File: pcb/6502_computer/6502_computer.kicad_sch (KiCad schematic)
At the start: 44 parts, among them J1 Conn_02x04_Odd_Even, J2 USB_B, J3 Conn_02x20_Odd_Even, J4 Conn_01x04, J5 Conn_01x02, SW1 SW_Push, SW2 SW_Push, SW3 SW_Push, U1 6502, U10 CH340N, U11 MC6840, U2 6551, U3 74LS139, U4 74LS138, U5 CY62256-70PC, U6 27C64, U7 74LS00, U8 DS1813-5+, U9 74LS93, X1 ACO-xxxMHz, Y1 1.8432MHz

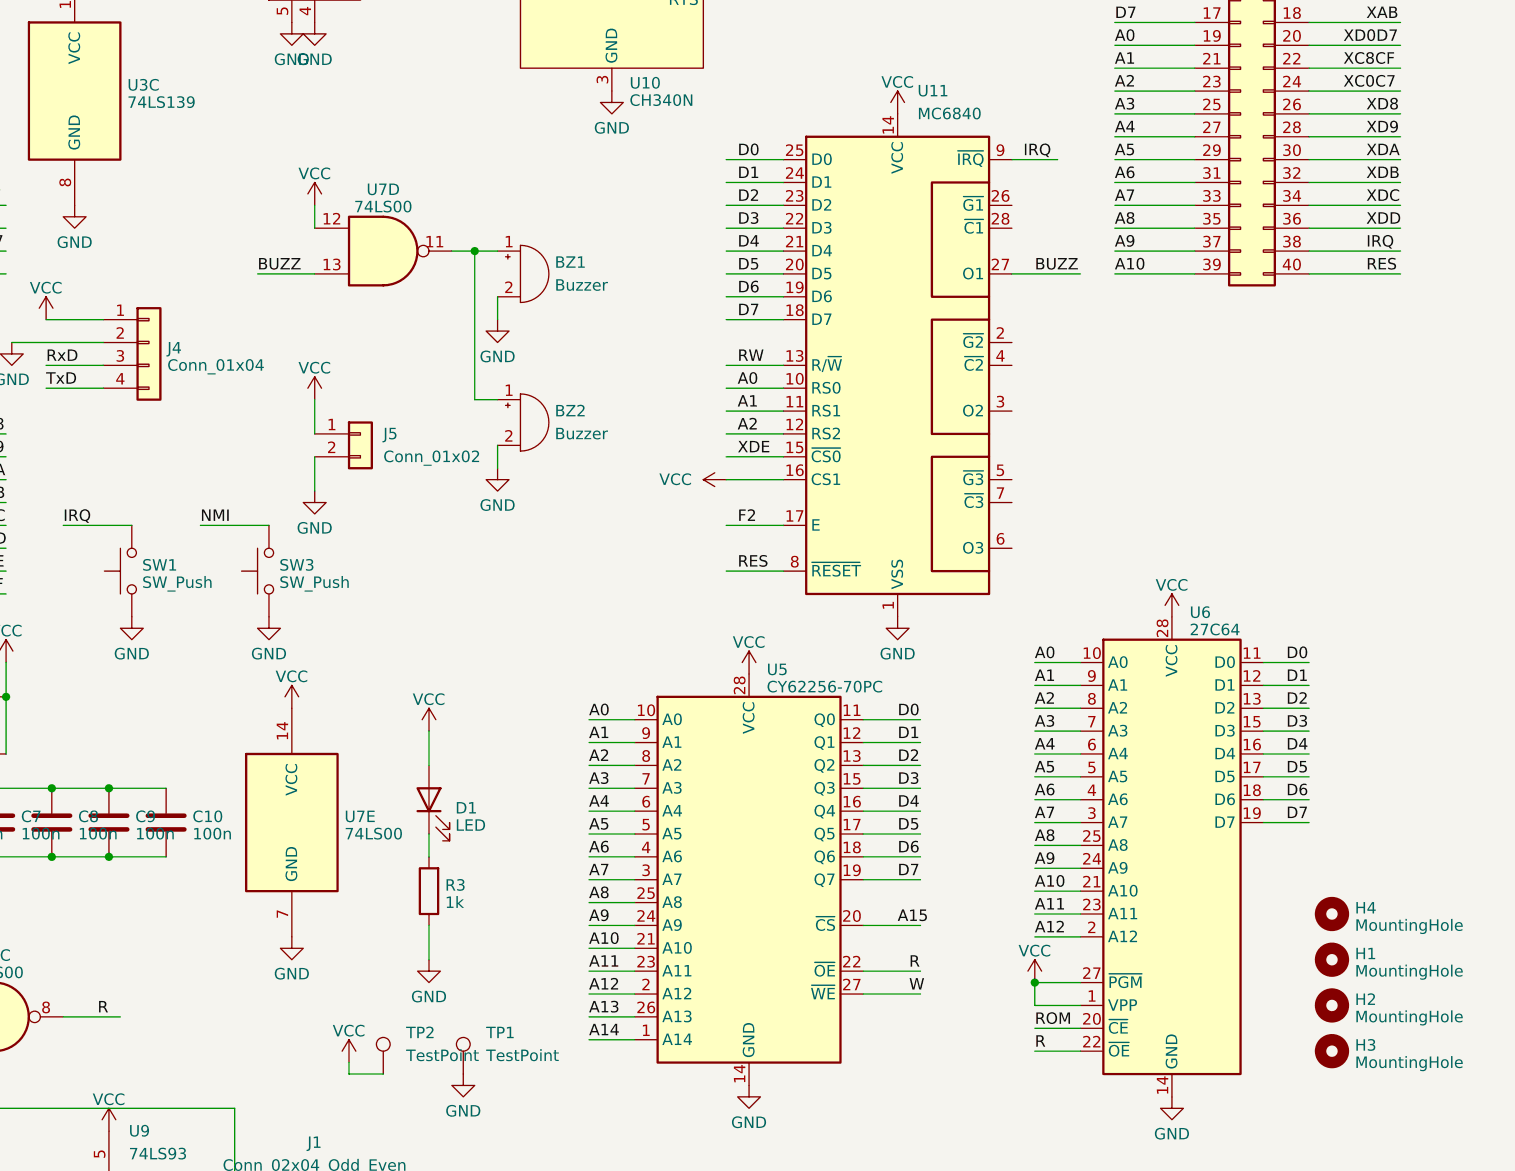
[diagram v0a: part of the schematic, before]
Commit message: added timer outputs from 6840
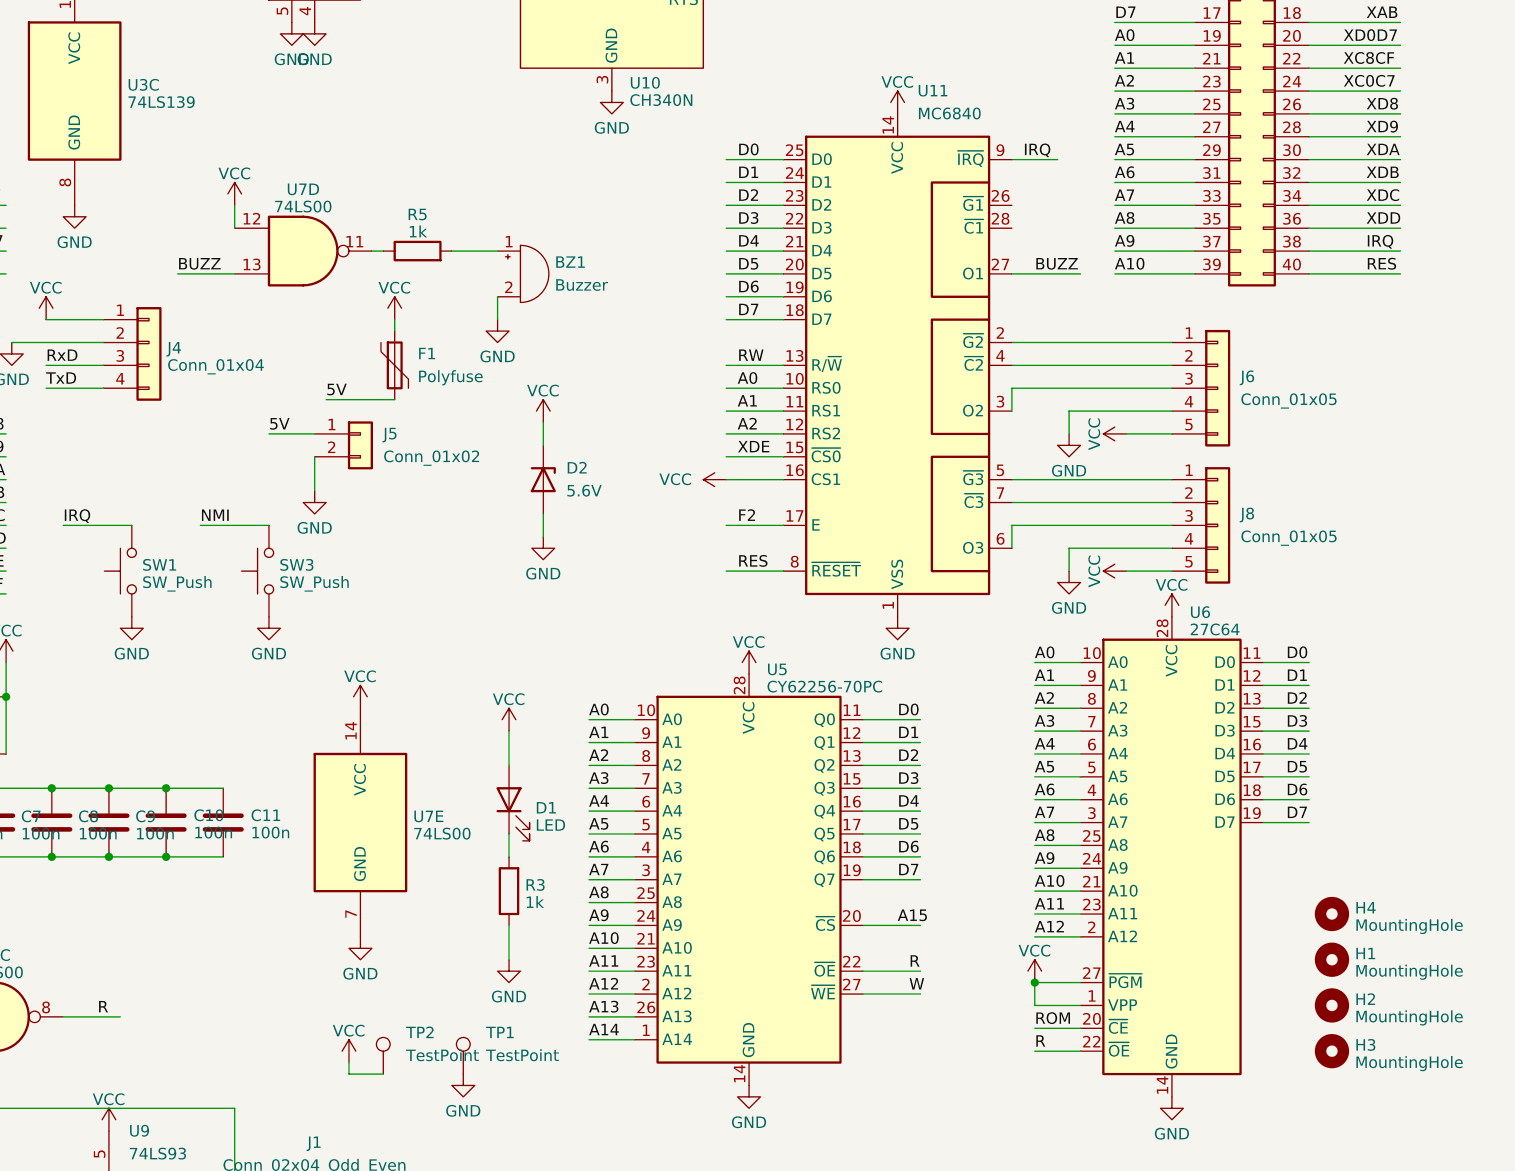
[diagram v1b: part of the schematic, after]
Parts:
- removed BZ2: Buzzer, Buzzer_Beeper:Buzzer_12x9.5RM7.6, symbol Device:Buzzer
- added C11: 100n, Capacitor_SMD:C_0805_2012Metric, symbol Device:C
- added D2: 5.6V, Diode_SMD:D_SOD-123, symbol Device:D_Zener
- added F1: Polyfuse, Fuse:Fuse_0805_2012Metric, symbol Device:Polyfuse
- added J6, J8: Conn_01x05, Connector_Molex:Molex_KK-254_AE-6410-05A_1x05_P2.54mm_Vertical, symbol Connector_Generic:Conn_01x05
- added R5: 1k, Resistor_SMD:R_0805_2012Metric, symbol Device:R
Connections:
- net GND: now also C11.1, D2.2 (A), J6.4 (Pin_4), J8.4 (Pin_4)
- net VCC: now also C11.2, D2.1 (K), F1.1, J6.5 (Pin_5), J8.5 (Pin_5); no longer J5.1 (Pin_1)
- net at U7.11: now also R5.1; no longer BZ1.1 (+)
- net at U11.2 (~{G2}): now also J6.1 (Pin_1)
- net at U11.3 (O2): now also J6.3 (Pin_3)
- net at U11.4 (~{C2}): now also J6.2 (Pin_2)
- net at U11.5 (~{G3}): now also J8.1 (Pin_1)
- net at U11.6 (O3): now also J8.3 (Pin_3)
- net at U11.7 (~{C3}): now also J8.2 (Pin_2)
- new net: BZ1.1 (+), R5.2
- new net 5V: F1.2, J5.1 (Pin_1)
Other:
- moved on the sheet: D1, R3, U7D, U7E

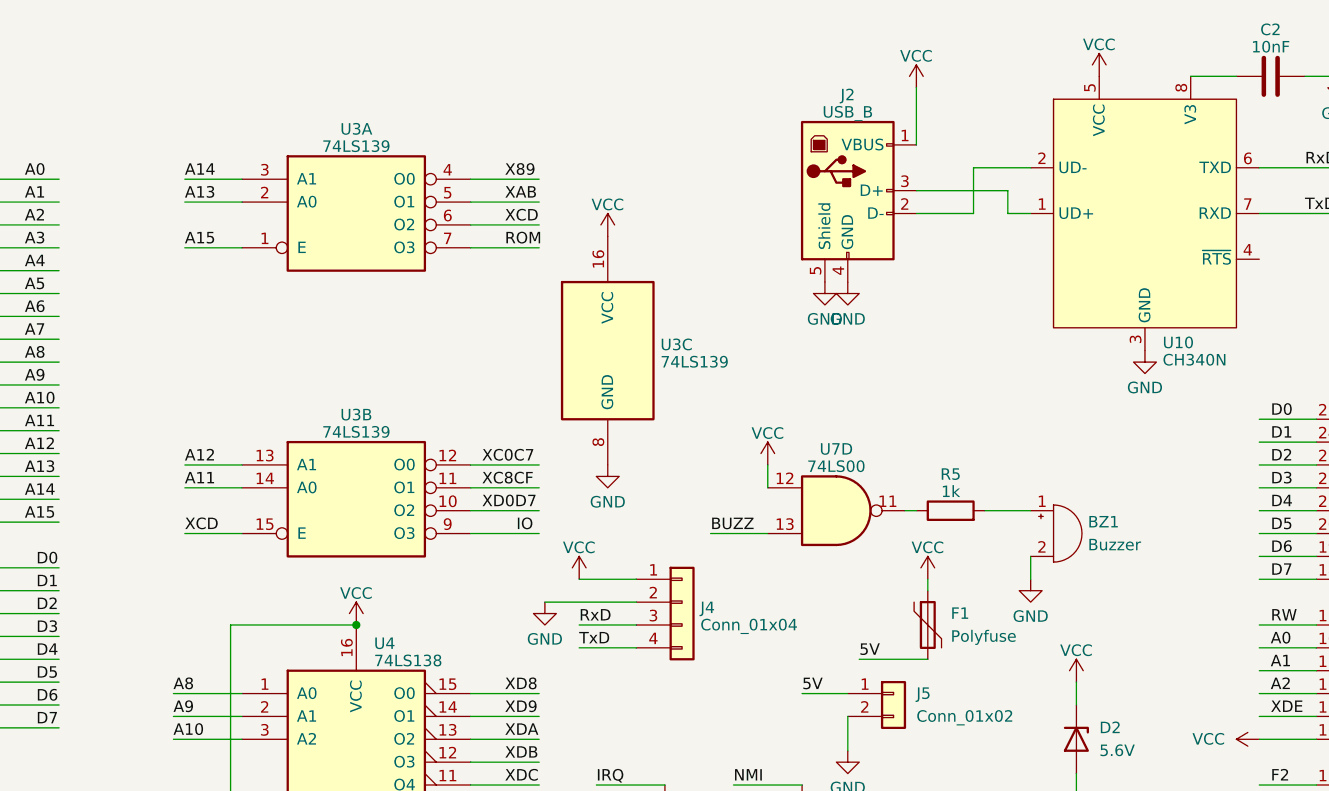
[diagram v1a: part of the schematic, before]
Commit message: fixed problem with not negating E for 74LS139. Buzzer is now using a transistor. 6502 is ZIF friendly.
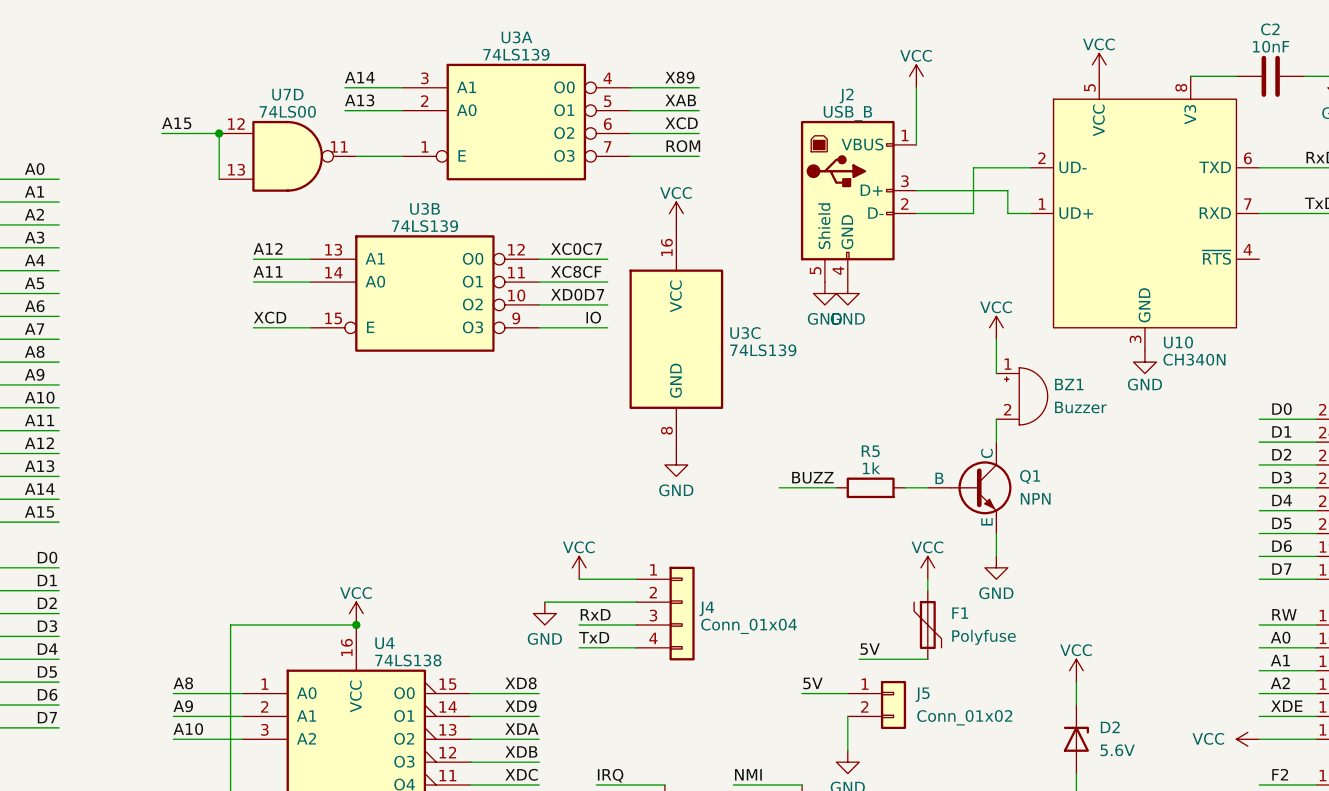
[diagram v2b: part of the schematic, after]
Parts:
- added Q1: NPN, Package_TO_SOT_SMD:TSOT-23, symbol Simulation_SPICE:NPN
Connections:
- net A15: now also U7.12, U7.13; no longer U3.1 (E)
- net BUZZ: now also R5.1; no longer U7.13
- net GND: now also Q1.3 (E); no longer BZ1.2 (-)
- net VCC: now also BZ1.1 (+); no longer U7.12
- net at U7.11: now also U3.1 (E); no longer R5.1
- net at R5.2: now also Q1.2 (B); no longer BZ1.1 (+)
- new net: BZ1.2 (-), Q1.1 (C)
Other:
- moved on the sheet: BZ1, R5, U3A, U3B, U3C, U7D

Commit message: v1.2 label fixes, pullup resistors for uart, routed
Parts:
- removed Q1: NPN, Package_TO_SOT_SMD:TSOT-23, symbol Simulation_SPICE:NPN
- added Q1: BC817, Package_TO_SOT_SMD:SOT-23, symbol Transistor_BJT:BC817
- added R10, R11, R12, R7, R8, R9: 10k, Resistor_SMD:R_0805_2012Metric, symbol Device:R
- added R5: 220, Resistor_SMD:R_0805_2012Metric, symbol Device:R
- U10: renamed from U11; footprint Package_DIP:DIP-28_W15.24mm -> Package_DIP:DIP-28_W15.24mm_LongPads
- renumbered C11 to C10, C2 to C11, C3 to C2, C4 to C3, C5 to C4, C6 to C5, C7 to C6, C8 to C7, C9 to C8, C10 to C9, D2 to D1, D1 to D2, H4 to H1, H1 to H2, H2 to H3, H3 to H4, J4 to J1, J1 to J2, J2 to J3, J5 to J4, J6 to J5, J8 to J6, J3 to J7, R4 to R1, R1 to R2, R2 to R3, R5 to R4, R3 to R6, SW2 to SW1, SW1 to SW2, TP2 to TP1, TP1 to TP2, U6 to U11, U8 to U3, U7 to U4, U4 to U5, U3 to U6, U9 to U7, U10 to U8, U5 to U9
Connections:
- net GND: now also Q1.2 (E), R10.2, R11.2, R12.2, R7.2, R8.2, R9.2
- net IRQ: now also U10.26 (~{G1}), R11.1
- net VCC: no longer U11.28 (VCC)
- net at J5.1 (Pin_1), U10.2 (~{G2}): now also R7.1
- net at U10.28 (~{C1}): now also R12.1
- net at J5.2 (Pin_2), U10.4 (~{C2}): now also R8.1
- net at J6.1 (Pin_1), U10.5 (~{G3}): now also R9.1
- net at J6.2 (Pin_2), U10.7 (~{C3}): now also R10.1
- net at R4.2: now also Q1.1 (B)
- net at BZ1.2 (-): now also R5.2
- new net: Q1.3 (C), R5.1
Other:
- moved on the sheet: BZ1, D1, F1, J5, J6, R4, U10
